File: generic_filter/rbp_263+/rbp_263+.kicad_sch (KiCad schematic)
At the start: 63 parts, among them J1 RF_IN, J10 +5V, J11 RF_OUT, J12 RF_OUT, J13 +5V, J14 VSHUT, J2 RF_OUT, J3 RF_IN, J4 RF_OUT, J5 RF_IN, J6 RF_OUT, J7 RF_IN, J8 RF_IN, J9 +5V, U1 RBP263+/RBP188+, U3 PHA-13LN

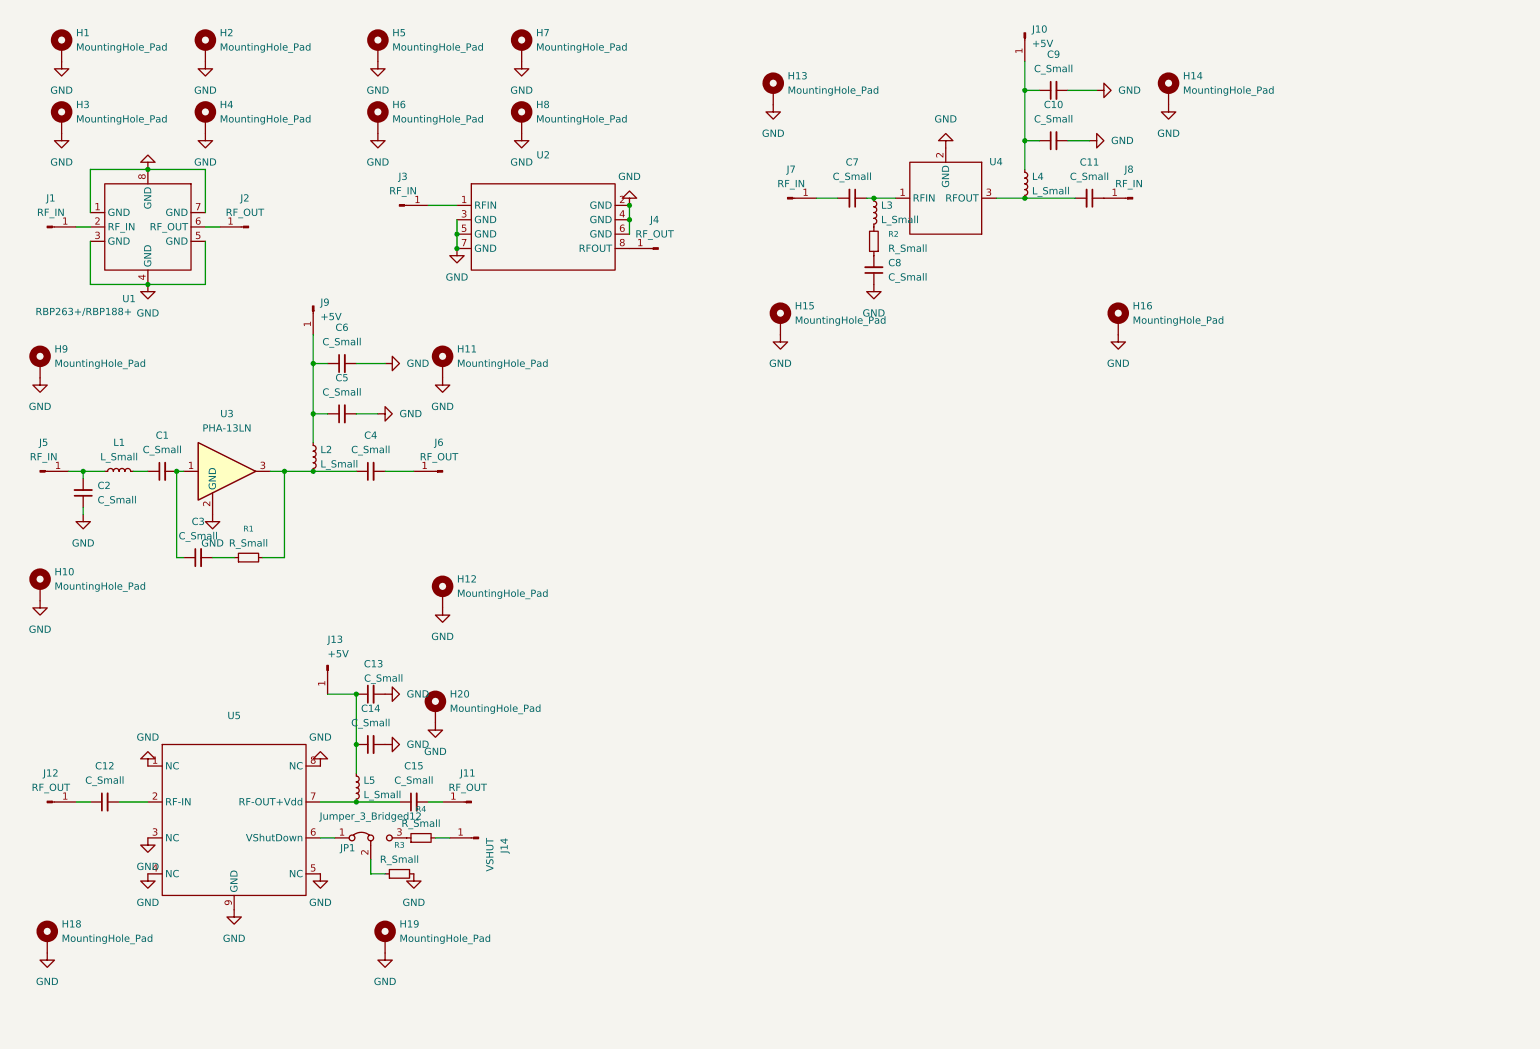
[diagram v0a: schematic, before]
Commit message: added gdt, tvs schematics and footprints
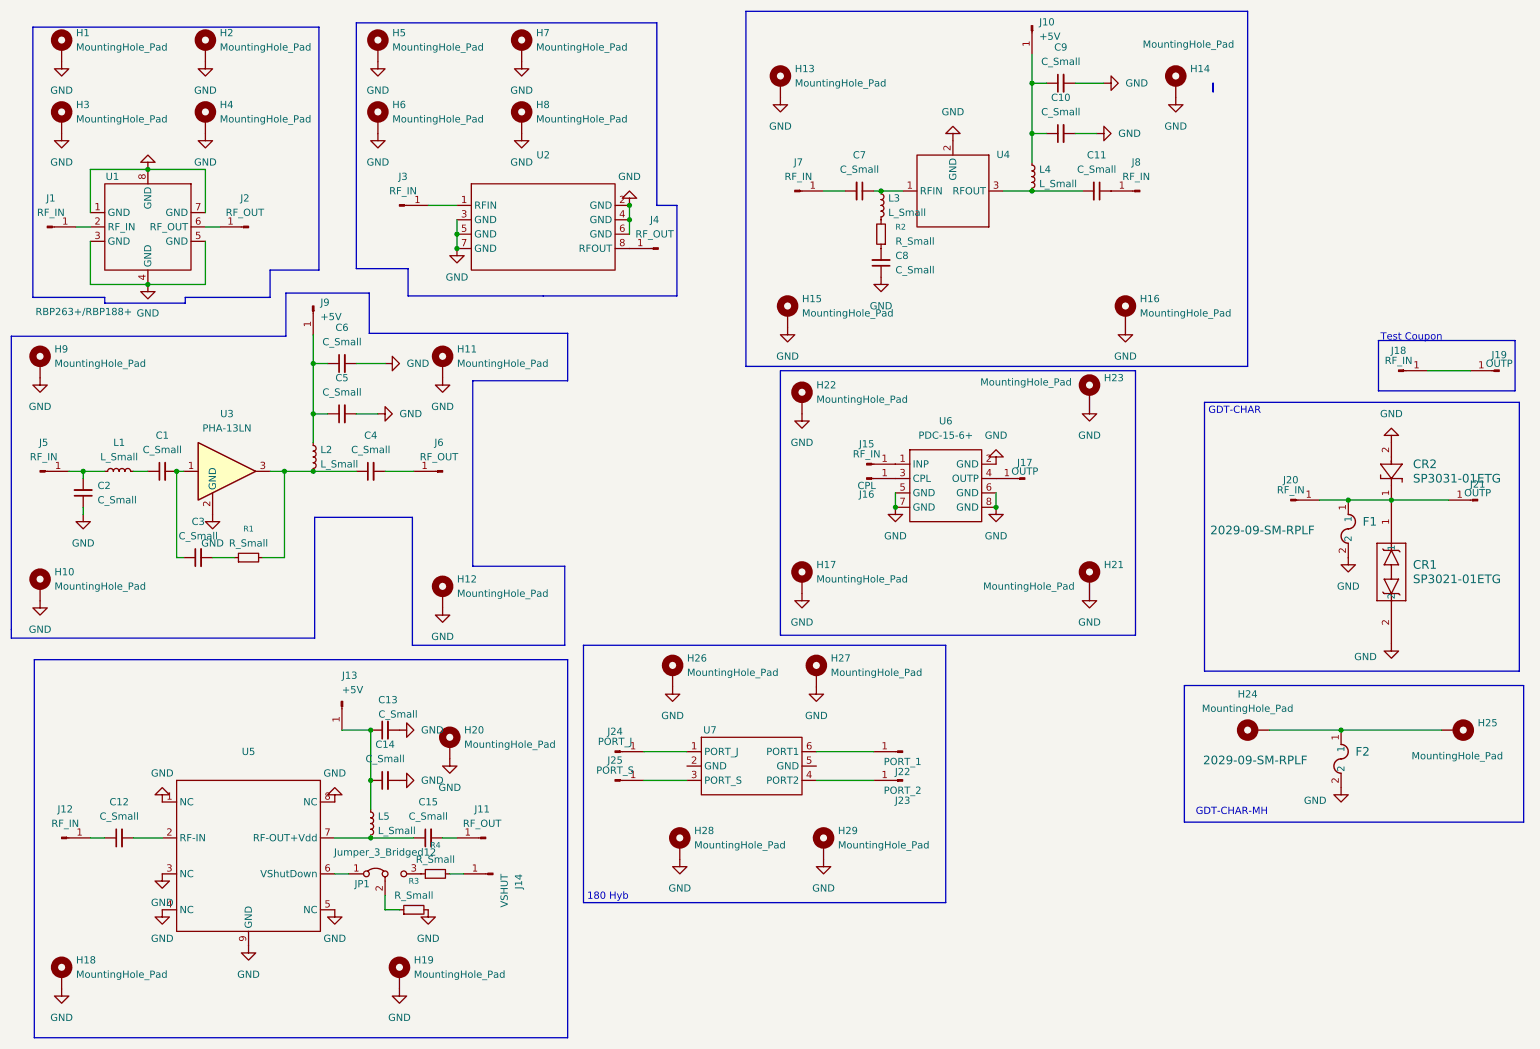
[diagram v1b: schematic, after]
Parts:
- added CR1: SP3021-01ETG, SOD882_LTF, symbol SP3021:SP3021-01ETG
- added CR2: SP3031-01ETG, SP3031:SOD882_LTF-L, symbol SP3031:SP3031-01ETG
- added F1, F2: 2029-09-SM-RPLF, FUSE_2029-09-SM-RPLF_BRN, symbol 2029-09-SMLF:2029-09-SM-RPLF
- added H17, H21, H22, H23, H26, H27, H28, H29: MountingHole_Pad, MountingHole:MountingHole_2.2mm_M2_DIN965_Pad, symbol Mechanical:MountingHole_Pad
- added H24, H25: MountingHole_Pad, MountingHole:MountingHole_2.7mm_M2.5_DIN965_Pad_TopBottom, symbol Mechanical:MountingHole_Pad
- added J15, J18, J20: RF_IN, PanelMountRF_DC:RF_SMA_Edge_PanelMount, symbol Connector:Conn_01x01_Pin
- added J16: CPL, PanelMountRF_DC:RF_SMA_Edge_PanelMount, symbol Connector:Conn_01x01_Pin
- added J17, J19, J21: OUTP, PanelMountRF_DC:RF_SMA_Edge_PanelMount, symbol Connector:Conn_01x01_Pin
- added J22: PORT_1, PanelMountRF_DC:RF_SMA_Edge_PanelMount, symbol Connector:Conn_01x01_Pin
- added J23: PORT_2, PanelMountRF_DC:RF_SMA_Edge_PanelMount, symbol Connector:Conn_01x01_Pin
- added J24: PORT_J, PanelMountRF_DC:RF_SMA_Edge_PanelMount, symbol Connector:Conn_01x01_Pin
- added J25: PORT_S, PanelMountRF_DC:RF_SMA_Edge_PanelMount, symbol Connector:Conn_01x01_Pin
- added U6: PDC-15-6+, minickts_kicad:Mini-Circuits_A01, symbol minicircuits:PDC-15-6+
- added U7: ~, minickts_kicad:Mini-Circuits_CD636_H4.11mm, symbol minicircuits:AMT-32+
- J12: value RF_OUT -> RF_IN
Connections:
- net GND: now also CR1.2, CR2.2, F1.2, F2.2, H17.1, H21.1, H22.1, H23.1, H26.1, H27.1, H28.1, H29.1, U6.2 (GND), U6.5 (GND), U6.6 (GND), U6.7 (GND), U6.8 (GND)
- new net: CR1.1, CR2.1, F1.1, J20.1 (Pin_1), J21.1 (Pin_1)
- new net: J18.1 (Pin_1), J19.1 (Pin_1)
- new net: F2.1, H24.1, H25.1
- new net: J22.1 (Pin_1), U7.6 (PORT1)
- new net: J23.1 (Pin_1), U7.4 (PORT2)
- new net: J24.1 (Pin_1), U7.1 (PORT_J)
- new net: J25.1 (Pin_1), U7.3 (PORT_S)
- new net: J15.1 (Pin_1), U6.1 (INP)
- new net: J16.1 (Pin_1), U6.3 (CPL)
- new net: J17.1 (Pin_1), U6.4 (OUTP)
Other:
- note added: "180 Hyb"
- note added: "GDT-CHAR"
- note added: "GDT-CHAR-MH"
- note added: "Test Coupon"
- moved on the sheet: C10, C11, C12, C13, C14, C15, C7, C8, C9, H13, H14, H15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

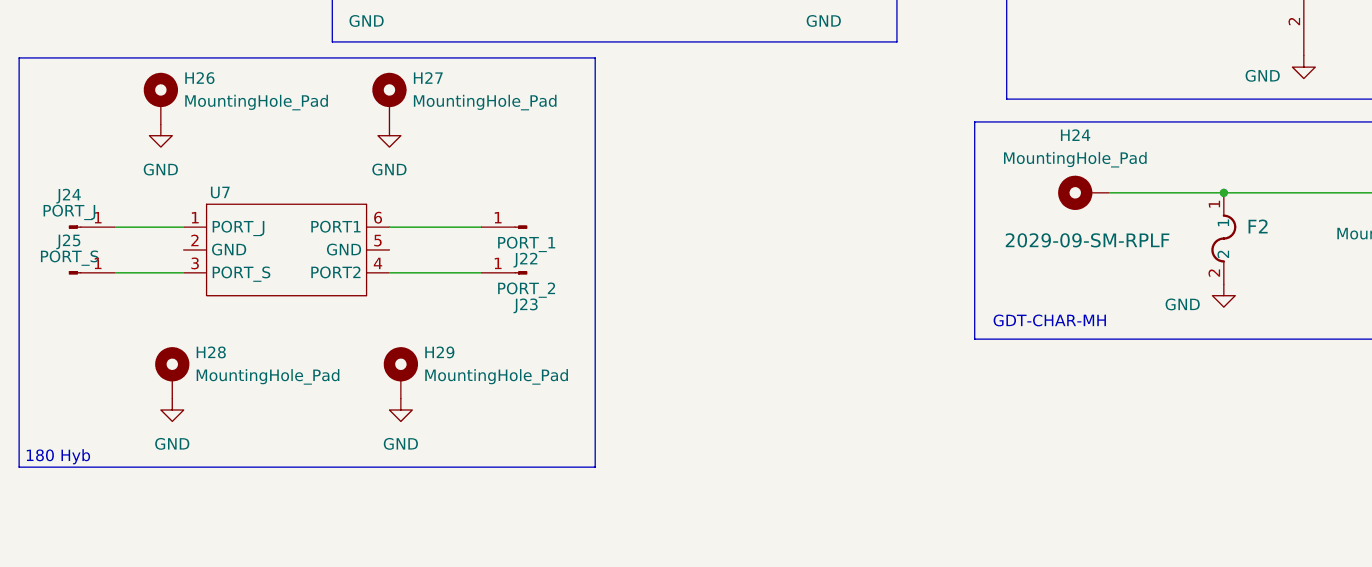
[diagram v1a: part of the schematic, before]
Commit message: Updated by jayasandhya
via stitched,
2 pcbs updated
solder mask removed
layout slightly changed for optimization
mouse bits added - panelized
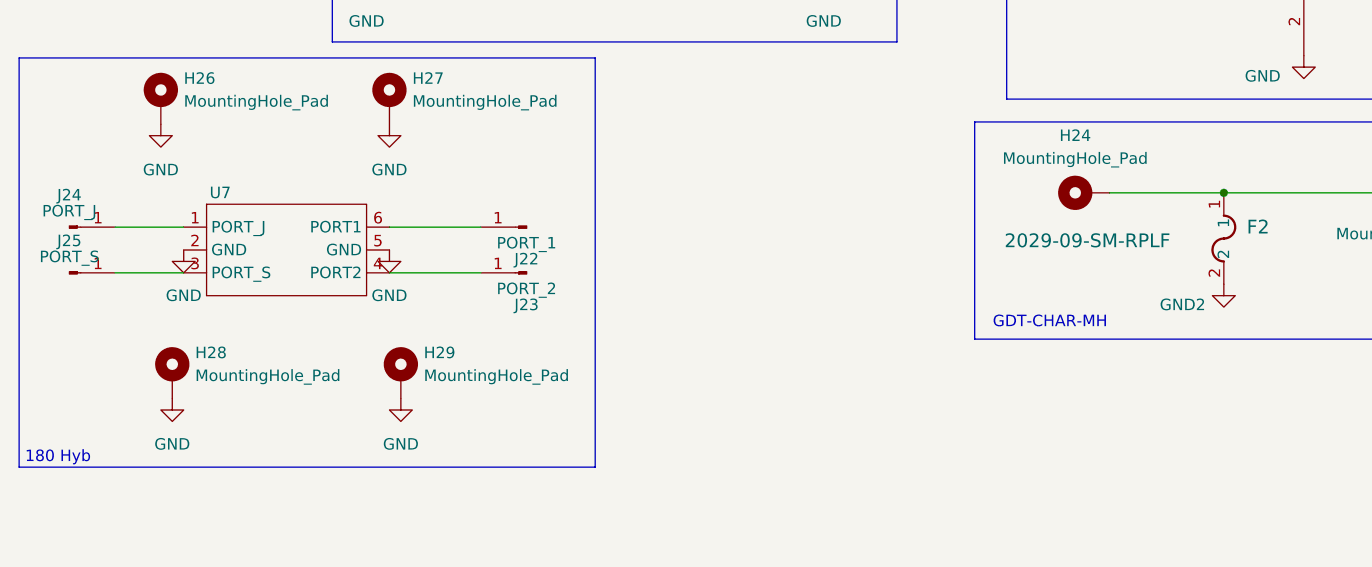
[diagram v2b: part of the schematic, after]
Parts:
- CR1: footprint SOD882_LTF -> SP3021:SOD882_LTF
- U2: footprint minickts_kicad:Mini-Circuits_HF1139_LandPatternPL-230 -> RF_Mini-Circuits:Mini-Circuits_HF1139
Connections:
- net GND: now also U7.2 (GND), U7.5 (GND); no longer F2.2
- new net GND2: F2.2
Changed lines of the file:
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@@
 			)
 		)
-		(property "Value" "GND"
+		(property "Value" "GND2"
 			(at 243.078 152.146 0)
 			(effects
@@
 			)
 		)
-		(property "Footprint" "minickts_kicad:Mini-Circuits_HF1139_LandPatternPL-230"
+		(property "Footprint" "RF_Mini-Circuits:Mini-Circuits_HF1139"
 			(at 106.68 50.8 0)
 			(effects
@@
 	(symbol
 		(lib_id "power:GND")
+		(at 154.94 146.05 0)
+		(unit 1)
+		(exclude_from_sim no)
+		(in_bom yes)
+		(on_board yes)
+		(dnp no)
+		(fields_autoplaced yes)
+		(property "Reference" "#PWR057"
+			(at 154.94 152.4 0)
+			(effects
+				(font
+					(size 1.27 1.27)
+				)
+				(hide yes)
+			)
+		)
+		(property "Value" "GND"
+			(at 154.94 151.13 0)
+			(effects
+				(font
+					(size 1.27 1.27)
+				)
+			)
+		)
+		(property "Footprint" ""
+			(at 154.94 146.05 0)
+			(effects
+				(font
+					(size 1.27 1.27)
+				)
+				(hide yes)
+			)
+		)
+		(property "Datasheet" ""
+			(at 154.94 146.05 0)
+			(effects
+				(font
+					(size 1.27 1.27)
+				)
+				(hide yes)
+			)
+		)
+		(property "Description" "Power symbol creates a global label with name \"GND\" , ground"
+			(at 154.94 146.05 0)
+			(effects
+				(font
+					(size 1.27 1.27)
+				)
+				(hide yes)
+			)
+		)
+		(pin "1"
+		)
+		(instances
+			(project "rbp_263+"
+				(path "/853aca7e-cbc0-4437-9dd1-d65fc429a4f3"
+					(reference "#PWR057")
+					(unit 1)
+				)
+			)
+		)
+	)
+	(symbol
+		(lib_id "power:GND")
 		(at 256.54 88.9 180)
 		(unit 1)
@@
 	(symbol
 		(lib_id "power:GND")
+		(at 132.08 146.05 0)
+		(unit 1)
+		(exclude_from_sim no)
+		(in_bom yes)
+		(on_board yes)
+		(dnp no)
+		(fields_autoplaced yes)
+		(property "Reference" "#PWR056"
+			(at 132.08 152.4 0)
+			(effects
+				(font
+					(size 1.27 1.27)
+				)
+				(hide yes)
+			)
+		)
+		(property "Value" "GND"
+			(at 132.08 151.13 0)
+			(effects
+				(font
+					(size 1.27 1.27)
+				)
+			)
+		)
+		(property "Footprint" ""
+			(at 132.08 146.05 0)
+			(effects
+				(font
+					(size 1.27 1.27)
+				)
+				(hide yes)
+			)
+		)
+		(property "Datasheet" ""
+			(at 132.08 146.05 0)
+			(effects
+				(font
+					(size 1.27 1.27)
+				)
+				(hide yes)
+			)
+		)
+		(property "Description" "Power symbol creates a global label with name \"GND\" , ground"
+			(at 132.08 146.05 0)
+			(effects
+				(font
+					(size 1.27 1.27)
+				)
+				(hide yes)
+			)
+		)
+		(pin "1"
+		)
+		(instances
+			(project "rbp_263+"
+				(path "/853aca7e-cbc0-4437-9dd1-d65fc429a4f3"
+					(reference "#PWR056")
+					(unit 1)
+				)
+			)
+		)
+	)
+	(symbol
+		(lib_id "power:GND")
 		(at 91.44 54.61 0)
 		(unit 1)
@@
 			)
 		)
-		(property "Footprint" "SOD882_LTF"
+		(property "Footprint" "SP3021:SOD882_LTF"
 			(at 256.54 99.06 0)
 			(effects
